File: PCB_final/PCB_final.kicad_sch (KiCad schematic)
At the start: 106 parts, among them J1 02x30_Shift_Register_Connector, J2 02x30_ADC_Connector, U1 74HC595, U2 74HC595, U3 74HC595, U4 74HC595, U5 74HC595, U6 74HC595, U7 74HC595, U8 MAX11643EEG, U9 MAX11643EEG

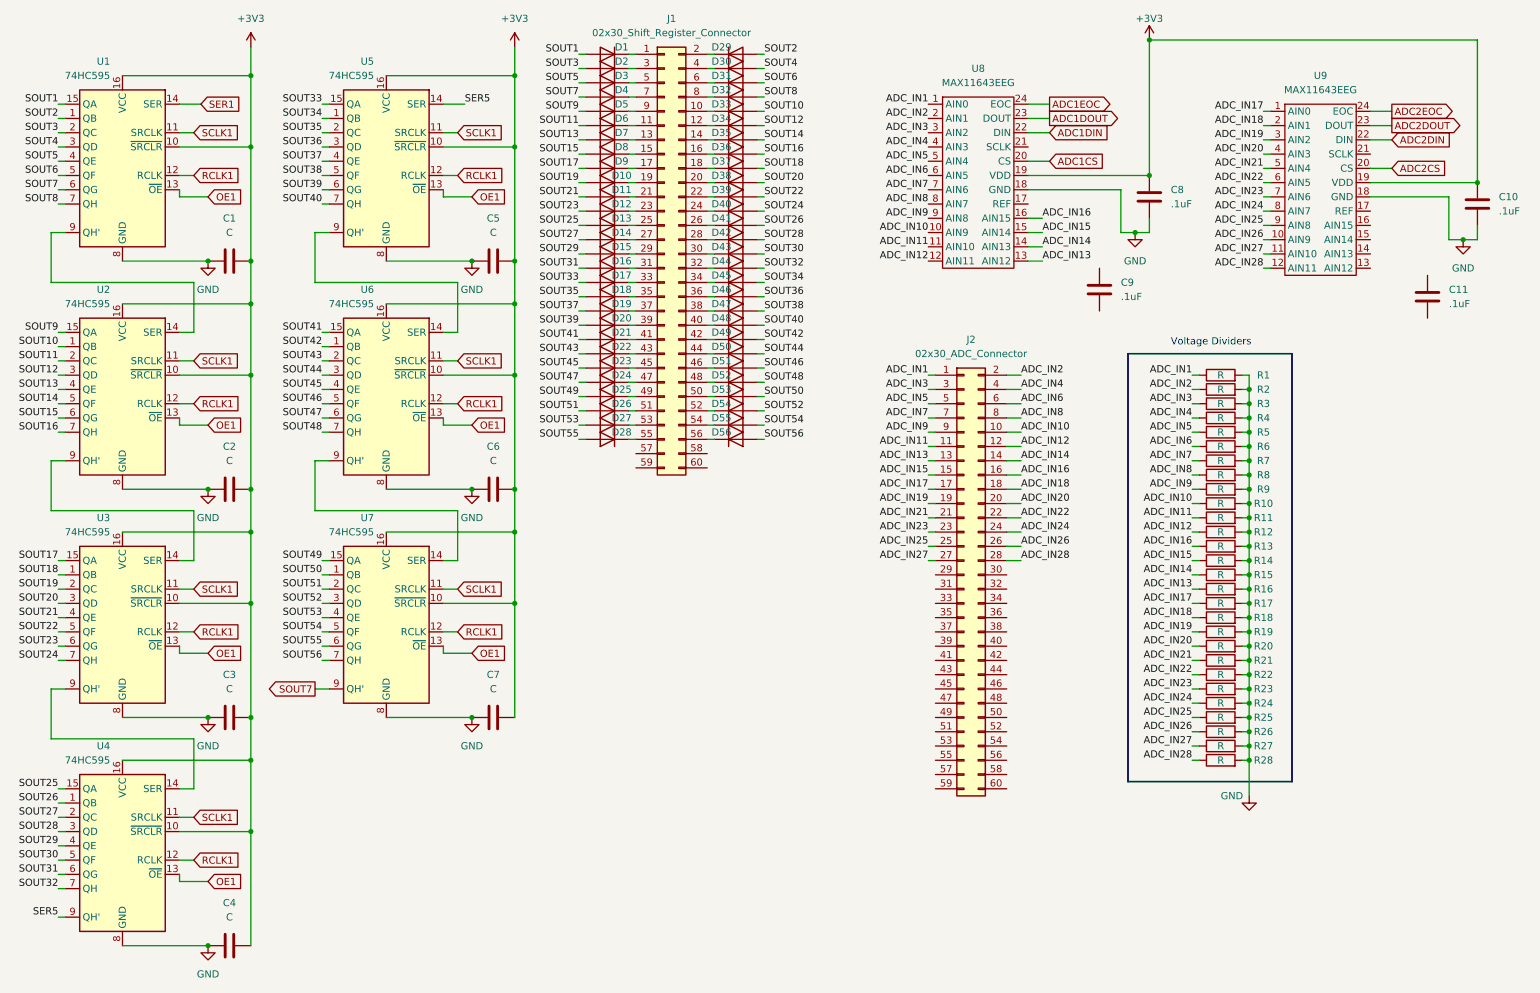
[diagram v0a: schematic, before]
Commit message: Separated RP2040 and interface board components into multiple sheets
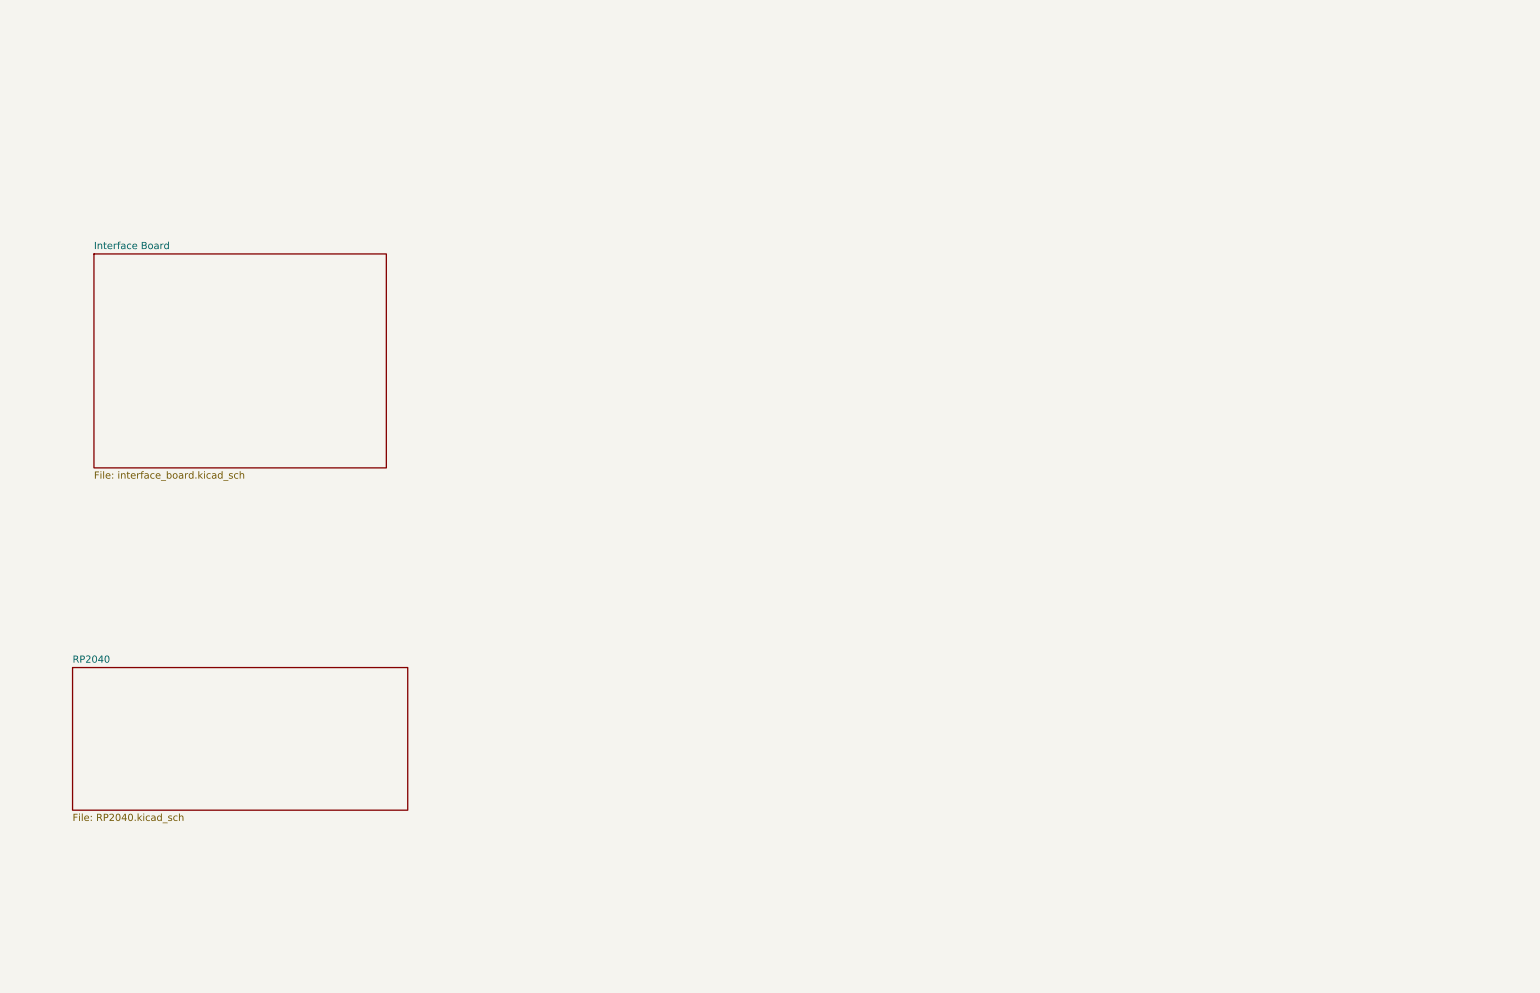
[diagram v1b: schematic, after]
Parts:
- removed C1, C2, C3, C4, C5, C6, C7: C, symbol Device:C
- removed C10, C11, C8, C9: .1uF, symbol Device:C
- removed D1, D10, D11, D12, D13, D14, D15, D16, D17, D18, D19, D2, D20, D21, D22, D23, D24, D25, D26, D27, D28, D29, D3, D30, D31, D32, D33, D34, D35, D36, D37, D38, D39, D4, D40, D41, D42, D43, D44, D45, D46, D47, D48, D49, D5, D50, D51, D52, D53, D54, D55, D56, D6, D7, D8, D9: D, symbol Device:D
- removed J1: 02x30_Shift_Register_Connector, symbol Connector_Generic:Conn_02x30_Odd_Even
- removed J2: 02x30_ADC_Connector, symbol Connector_Generic:Conn_02x30_Odd_Even
- removed R1, R10, R11, R12, R13, R14, R15, R16, R17, R18, R19, R2, R20, R21, R22, R23, R24, R25, R26, R27, R28, R3, R4, R5, R6, R7, R8, R9: R, symbol Device:R
- removed U1, U2, U3, U4, U5, U6, U7: 74HC595, symbol 74xx:74HC595
- removed U8, U9: MAX11643EEG, symbol Capstone_Library:MAX11643EEG
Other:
- added sheet Interface Board (interface_board.kicad_sch)
- added sheet RP2040 (RP2040.kicad_sch)
- note removed: "Voltage Dividers"
- company: (none) -> https://github.com/yoctometric/pressure-mat
- title: (none) -> ECE406 Pressure Mat Interface PCB

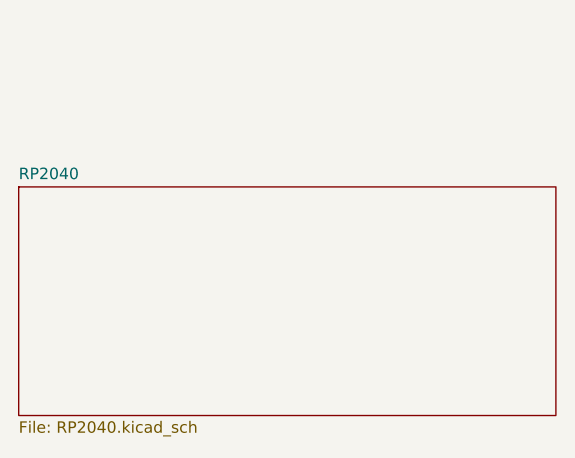
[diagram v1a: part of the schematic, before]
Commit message: beautified shift registers by putting decoupling capacitors as external elements and put in actual capacitor values
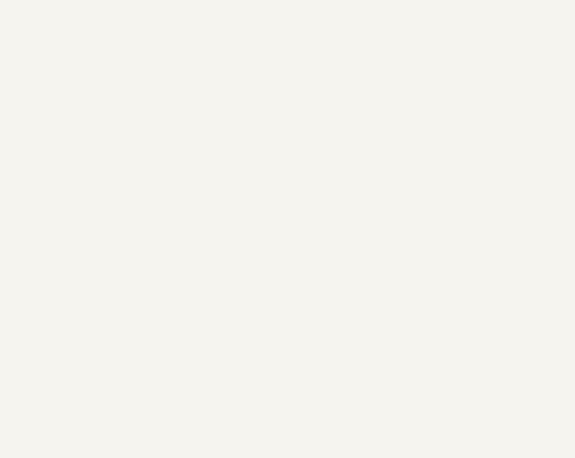
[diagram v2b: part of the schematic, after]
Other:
- removed sheet RP2040
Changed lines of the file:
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@@
     (company "https://github.com/yoctometric/pressure-mat")
-  )
-  (sheet (at 26.67 130.81) (size 59.69 25.4) (fields_autoplaced)
-    (stroke (width 0.1524) (type solid))
-    (fill (color 0 0 0 0.0000))
-    (property "Sheetname" "RP2040" (at 26.67 130.0984 0)
-      (effects (font (size 1.27 1.27)) (justify left bottom))
-    )
-    (property "Sheetfile" "RP2040.kicad_sch" (at 26.67 156.7946 0)
-      (effects (font (size 1.27 1.27)) (justify left top))
-    )
-    (instances
-      (project "PCB_final"
-        (path "/e4192969-4b4c-4bbf-a0a8-ef09d84e64d7" (page "2"))
-      )
-    )
   )
   (sheet (at 30.48 57.15) (size 52.07 38.1) (fields_autoplaced)

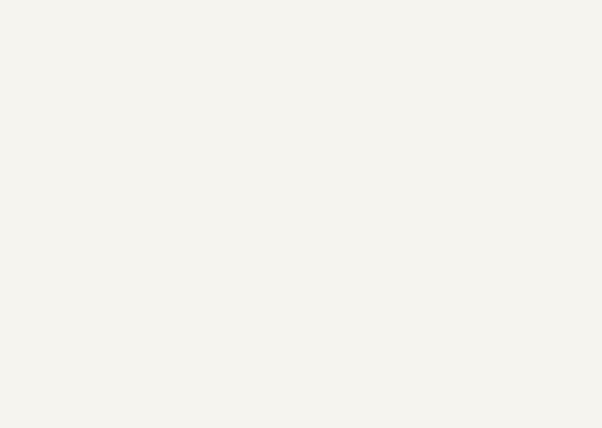
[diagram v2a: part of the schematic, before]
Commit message: Moved active low pass op-amp filter to its own schematic sheet
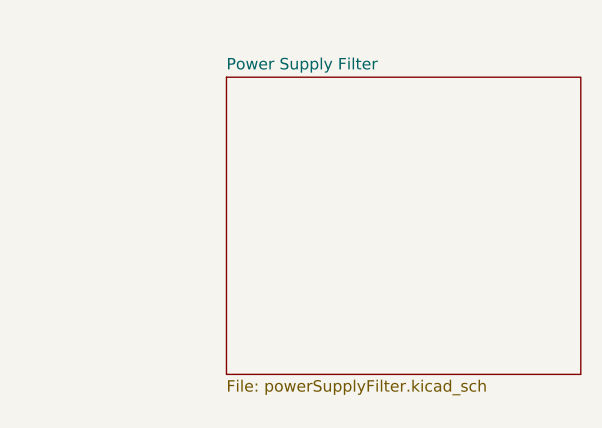
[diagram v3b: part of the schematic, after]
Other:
- added sheet Power Supply Filter (powerSupplyFilter.kicad_sch)
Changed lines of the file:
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@@
     (company "https://github.com/yoctometric/pressure-mat")
+  )
+  (sheet (at 110.49 60.96) (size 39.37 33.02) (fields_autoplaced)
+    (stroke (width 0.1524) (type solid))
+    (fill (color 0 0 0 0.0000))
+    (property "Sheetname" "Power Supply Filter" (at 110.49 60.2484 0)
+      (effects (font (size 1.27 1.27)) (justify left bottom))
+    )
+    (property "Sheetfile" "powerSupplyFilter.kicad_sch" (at 110.49 94.5646 0)
+      (effects (font (size 1.27 1.27)) (justify left top))
+    )
+    (instances
+      (project "PCB_final"
+        (path "/e4192969-4b4c-4bbf-a0a8-ef09d84e64d7" (page "3"))
+      )
+    )
   )
   (sheet (at 30.48 57.15) (size 52.07 38.1) (fields_autoplaced)
